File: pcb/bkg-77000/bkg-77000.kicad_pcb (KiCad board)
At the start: 2 copper layers, 203.2 x 114.3 mm, 480 parts

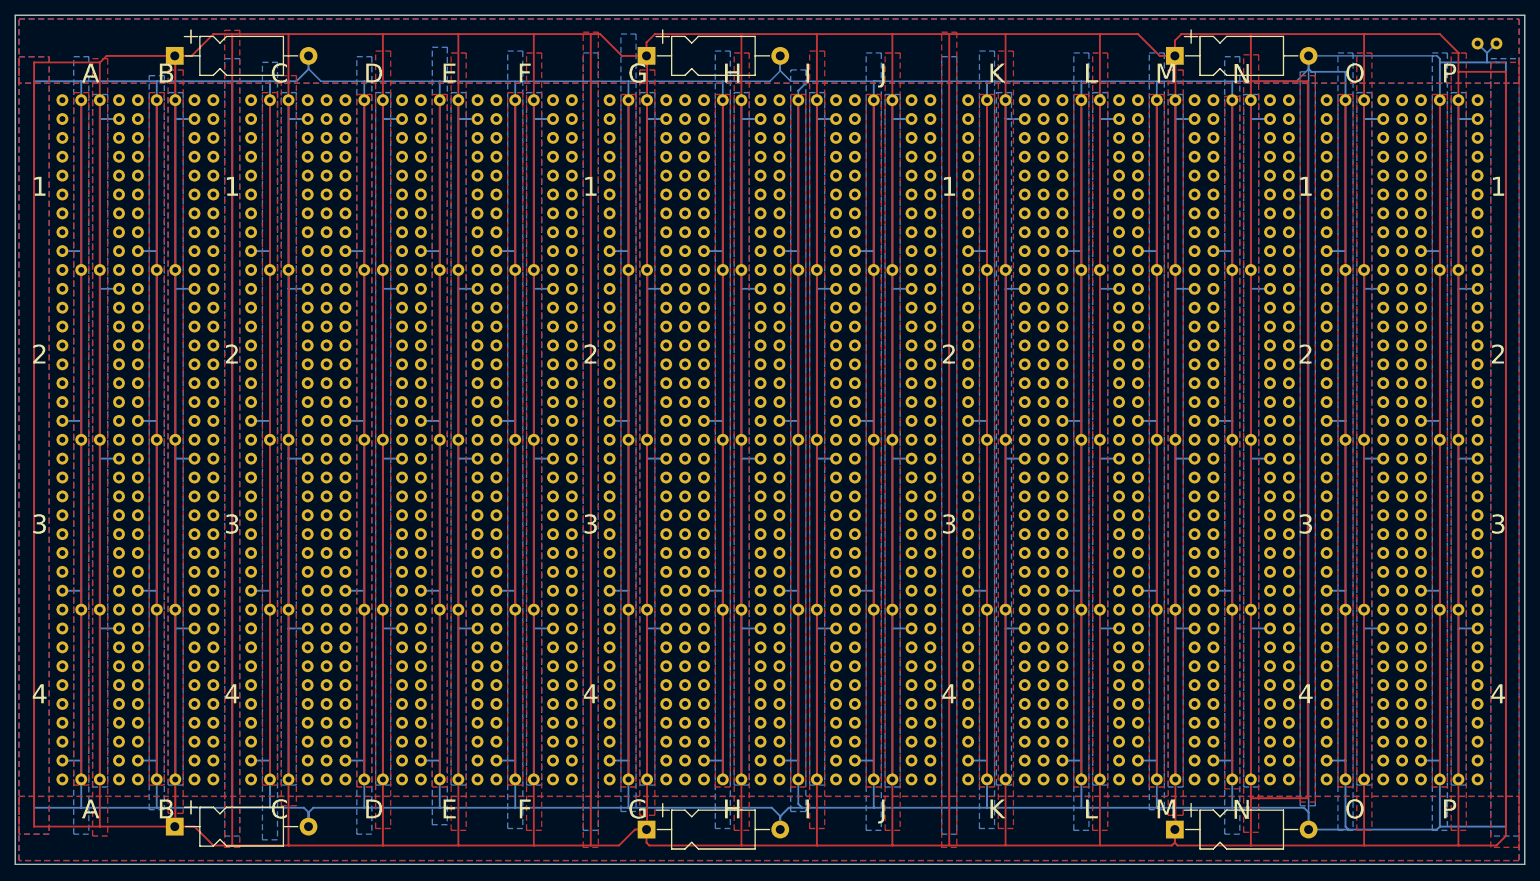
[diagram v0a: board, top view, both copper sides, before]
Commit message: bkg-77000: make DIP16 vcc/gnd traces thicker, do some cleanup.
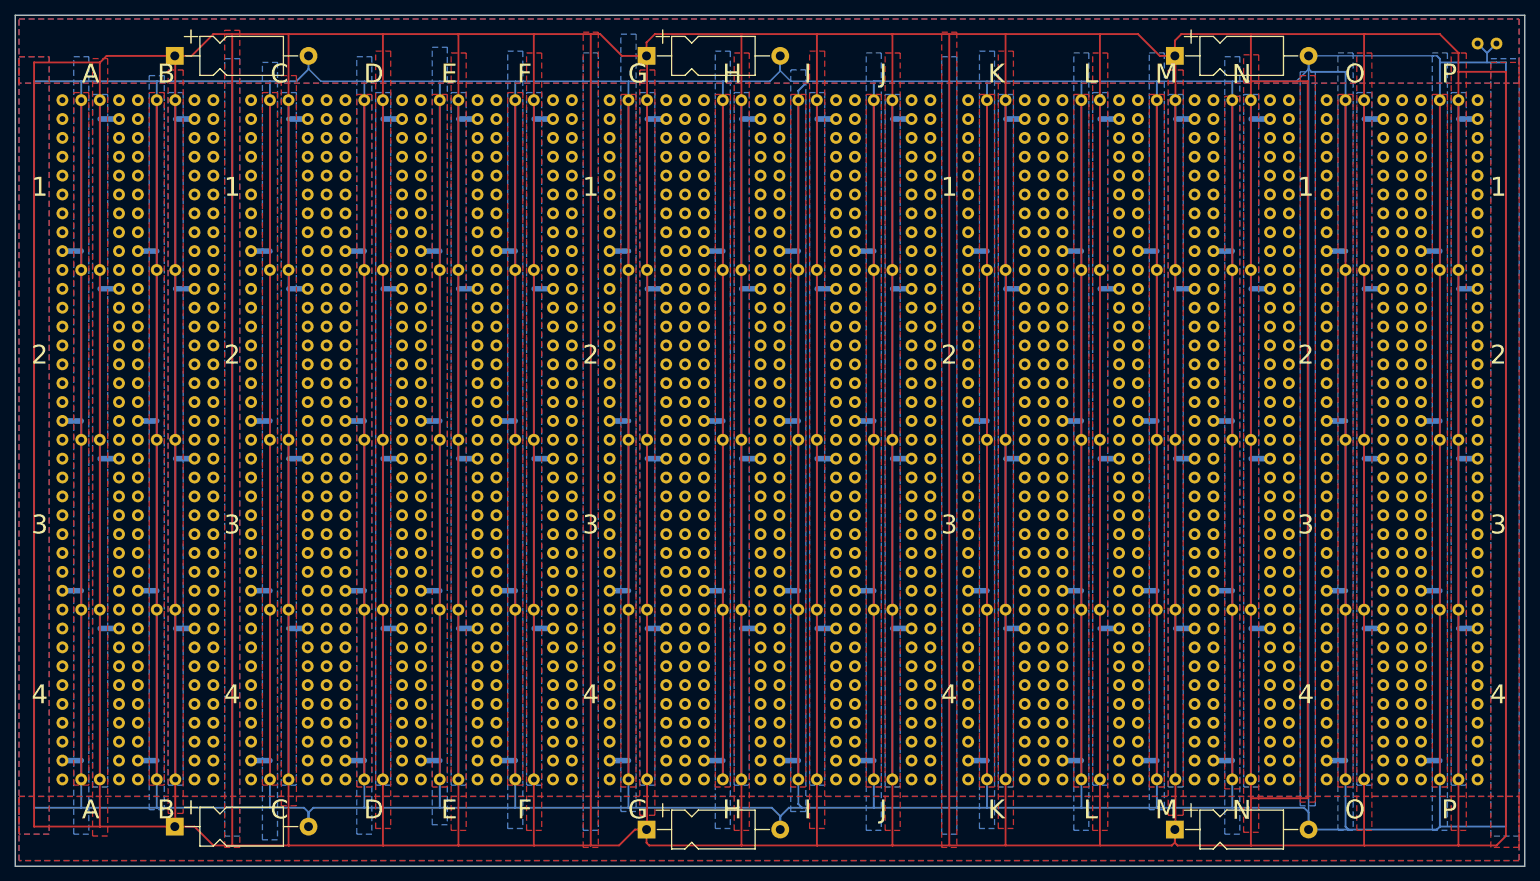
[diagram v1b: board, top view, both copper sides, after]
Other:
- board size 203.2 x 114.3 mm -> 203.2 x 114.6 mm

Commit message: bkg-7000: add more filter caps/power connection options, add space for I/O connectors/headers.
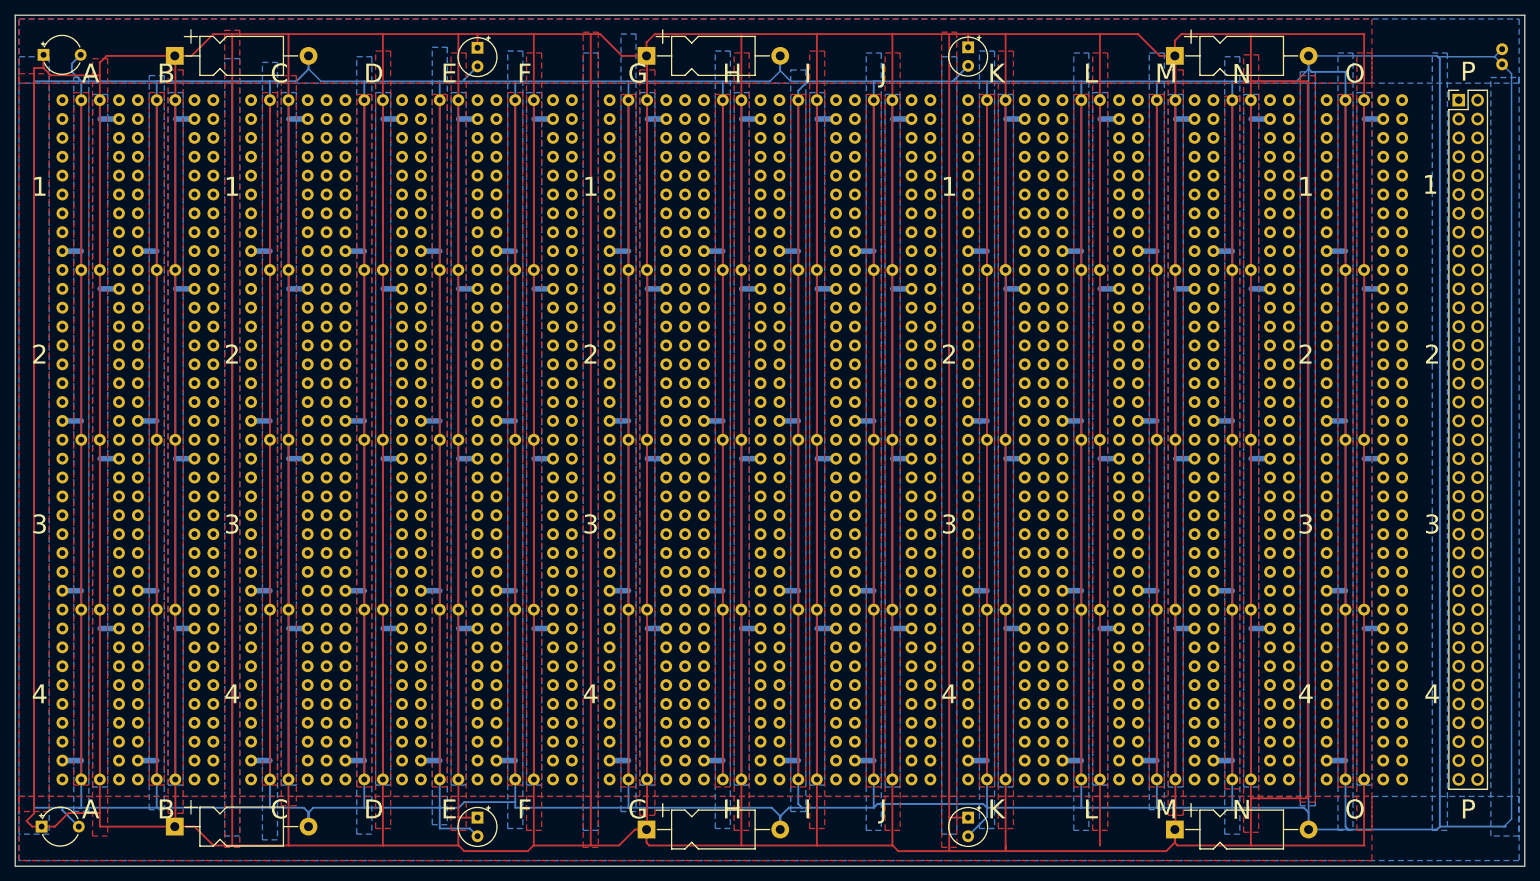
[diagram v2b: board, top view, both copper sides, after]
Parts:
- removed the ? at (222.2, 128.3)
- removed the ? at (214.6, 128.3)
- removed the REF** at (214.6, 108.0)
- removed the REF** at (214.6, 62.2)
- removed the REF** at (217.2, 36.8)
- removed the REF** at (214.6, 85.1)
- removed the REF** at (214.6, 39.4)
- removed the REF** at (217.2, 82.5)
- removed the REF** at (217.2, 59.7)
- removed the REF** at (217.2, 105.4)
- removed the REF** at (217.2, 128.3)
- added  : , Connector_PinHeader_2.54mm:PinHeader_2x37_P2.54mm_Vertical, F.Cu at (219.7, 36.8)
- added REF**: , Capacitor_THT:CP_Radial_Tantal_D5.0mm_P5.00mm, F.Cu at (29.2, 30.7)
- added REF**: , Capacitor_THT:CP_Radial_Tantal_D5.0mm_P5.00mm, F.Cu at (29.0, 134.6)
- added REF**: CP_Radial_Tantal_D5.0mm_P2.50mm, Capacitor_THT:CP_Radial_Tantal_D5.0mm_P2.50mm, F.Cu at (153.7, 29.7)
- added REF**: CP_Radial_Tantal_D5.0mm_P2.50mm, Capacitor_THT:CP_Radial_Tantal_D5.0mm_P2.50mm, F.Cu at (87.6, 29.8)
- added REF**: CP_Radial_Tantal_D5.0mm_P2.50mm, Capacitor_THT:CP_Radial_Tantal_D5.0mm_P2.50mm, F.Cu at (87.6, 133.4)
- added REF**: CP_Radial_Tantal_D5.0mm_P2.50mm, Capacitor_THT:CP_Radial_Tantal_D5.0mm_P2.50mm, F.Cu at (153.7, 133.4)
- moved ? 3.39 mm to (225.6, 30.0)
- moved ? 2.90 mm to (225.6, 32.0)
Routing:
- net VCC: track 4412.7 -> 4077.1 mm
- net GND: track 4227.0 -> 4151.3 mm
